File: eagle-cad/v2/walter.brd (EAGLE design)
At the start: 15.1 x 15.9 mm, 16 parts, among them U1 LP38511MRX-ADJ/NOPB, U2 LTC4054LES5-4.2TRPBF, U3 MLL1200STR

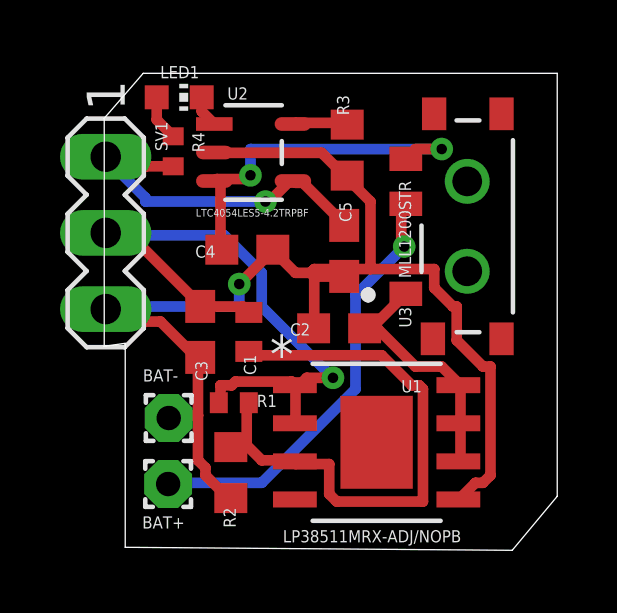
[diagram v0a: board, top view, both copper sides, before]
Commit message: board routing layout fixes
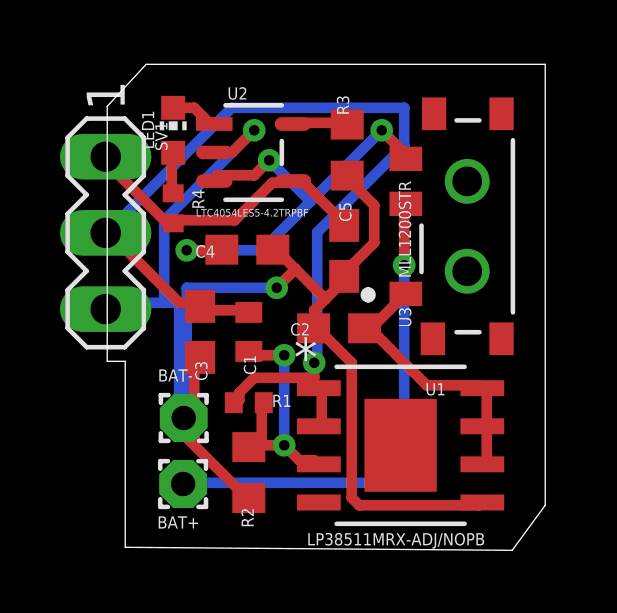
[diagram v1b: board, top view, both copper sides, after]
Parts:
- moved R4 1.90 mm to (2.30, 11.4)
- moved LED1 1.12 mm to (2.30, 14.0), turned to 0 degrees
- moved U1 0.81 mm to (9.88, 3.50)
- moved R2 0.60 mm to (4.82, 2.59)
- moved BAT+ 0.50 mm to (2.63, 2.21)
- moved BAT- 0.50 mm to (2.65, 4.41)
- moved R1 0.50 mm to (4.82, 4.92)
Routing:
- net N$4: track 19.4 -> 8.55 mm, vias 0 -> 2
- net N$3: track 22.0 -> 32.7 mm
- net GND: track 43.0 -> 49.9 mm, vias 1 -> 2
- net N$2: track 12.3 -> 14.7 mm, vias 2 -> 3
- net N$5: track 14.5 -> 16.7 mm
- net N$1: track 8.47 -> 9.52 mm
- net N$9: track 1.06 -> 1.58 mm
- net N$7: track 10.8 -> 10.2 mm, vias 1 -> 0
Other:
- board size 15.1 x 15.9 mm -> 14.6 x 16.2 mm
